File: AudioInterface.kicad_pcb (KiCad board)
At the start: 6 copper layers, 0 parts

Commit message: place component on pcb to generate bom
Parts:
- added D1: SML-P11UTT86R, LED_SMD:LED_0402_1005Metric, F.Cu at (146.7, 109.0)
- added D2: 1N4148, Diode_THT:D_DO-35_SOD27_P7.62mm_Horizontal, F.Cu at (154.9, 96.7)
- added D3: SML-P11MTT86RH, LED_SMD:LED_0402_1005Metric, F.Cu at (171.5, 90.3)
- added J3: PJ-393-8P, 0__:AUDIO-TH_PJ-393-8A, F.Cu at (143.8, 85.4)
- added J4: PJ-603, 0__:AUDIO-TH_PJ-603, F.Cu at (163.4, 69.6)
- added JP1: SolderJumper_2_Open, Jumper:SolderJumper-2_P1.3mm_Open_TrianglePad1.0x1.5mm, F.Cu at (151.2, 79.0)
- added JP2: SolderJumper_2_Open, Jumper:SolderJumper-2_P1.3mm_Open_TrianglePad1.0x1.5mm, F.Cu at (151.2, 82.5)
- added JP3: SolderJumper_2_Open, Jumper:SolderJumper-2_P1.3mm_Open_TrianglePad1.0x1.5mm, F.Cu at (151.2, 86.1)
- added JP4: SolderJumper_2_Open, Jumper:SolderJumper-2_P1.3mm_Open_TrianglePad1.0x1.5mm, F.Cu at (151.2, 89.6)
- added JP5: SolderJumper_2_Open, Jumper:SolderJumper-2_P1.3mm_Open_TrianglePad1.0x1.5mm, F.Cu at (151.2, 93.2)
- added JP6: SolderJumper_2_Open, Jumper:SolderJumper-2_P1.3mm_Open_TrianglePad1.0x1.5mm, F.Cu at (151.2, 96.7)
- added K1: IM03DGR, 0__:RELAY_IM03DGR, F.Cu at (159.1, 89.4)
- added Q1: AONS21321, 0__:DFN-8_L6.0-W5.0-P1.27-LS6.2-BL, F.Cu at (141.9, 104.2)
- added Q2: BC817, Package_TO_SOT_SMD:SOT-23, F.Cu at (167.3, 91.7)
- added S1: PG151101S11, 0__:SW_PG151101S11, F.Cu at (162.6, 80.9)
- added U2: ATTINY9-TS8R, 0__:SOT95P270X145-6N, F.Cu at (167.6, 87.0)
- added U3: L78L05ABUTR, 0__:L78L05ABUTR, F.Cu at (148.8, 104.0)
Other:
- board outline added: 71.5 x 73.5 mm

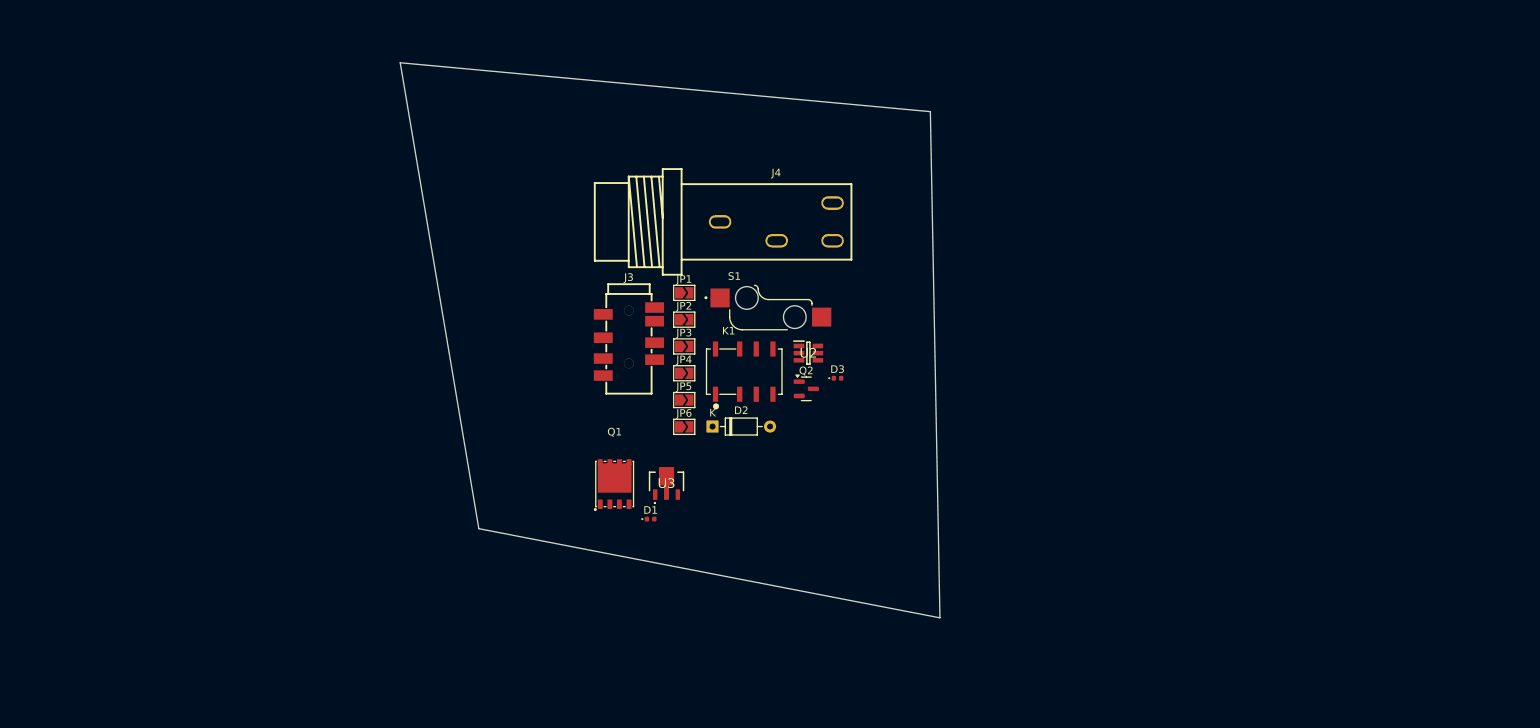
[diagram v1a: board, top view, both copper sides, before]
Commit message: source component and fix some lib
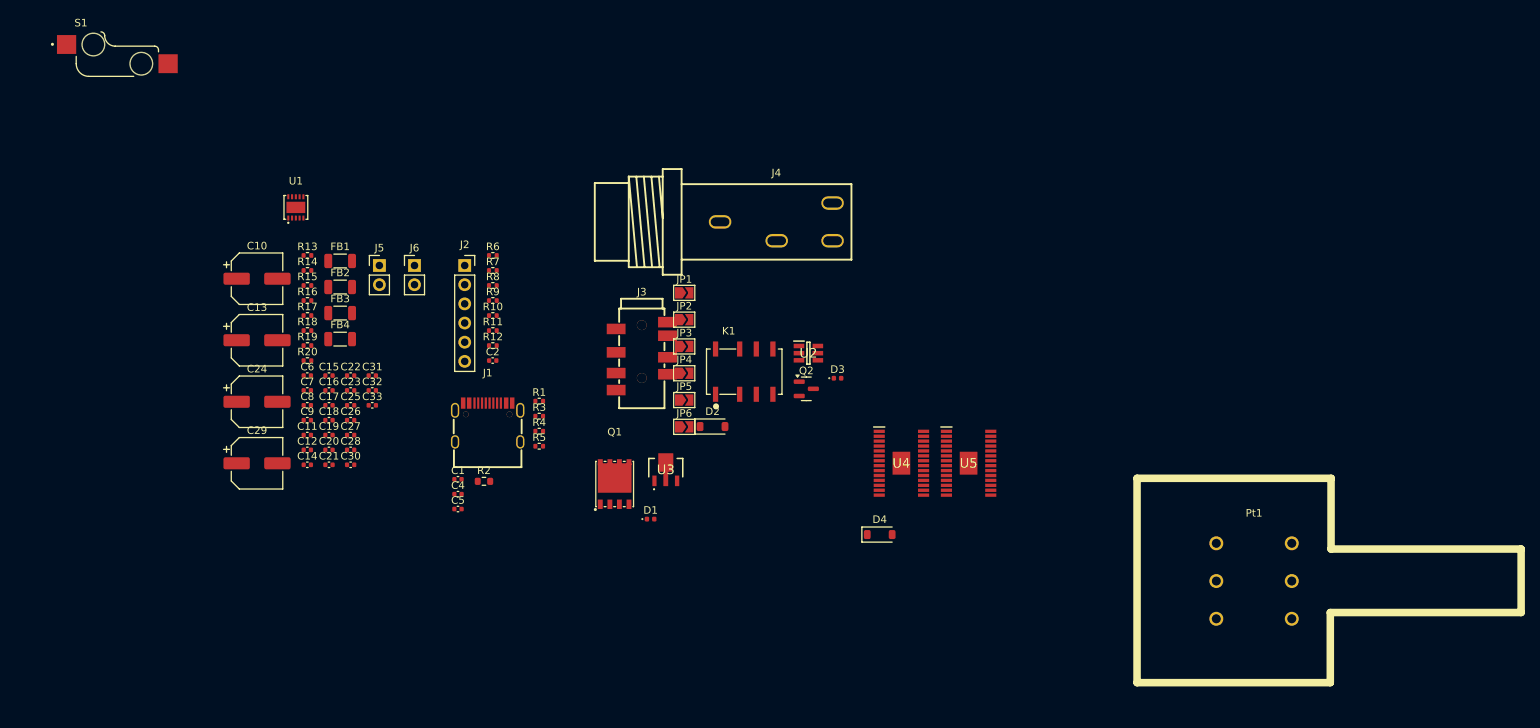
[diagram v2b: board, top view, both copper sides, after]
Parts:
- added C1: 1µ, Capacitor_SMD:C_0402_1005Metric, F.Cu at (121.2, 103.7)
- added C10: 100µ, Capacitor_SMD:CP_Elec_6.3x7.7, F.Cu at (94.6, 77.1)
- added C11: 100n, Capacitor_SMD:C_0402_1005Metric, F.Cu at (101.2, 97.8)
- added C12: 1n, Capacitor_SMD:C_0402_1005Metric, F.Cu at (101.2, 99.8)
- added C13: 100µ, Capacitor_SMD:CP_Elec_6.3x7.7, F.Cu at (94.6, 85.3)
- added C14: 100n, Capacitor_SMD:C_0402_1005Metric, F.Cu at (101.2, 101.8)
- added C15: 1n, Capacitor_SMD:C_0402_1005Metric, F.Cu at (104.1, 90.0)
- added C16: 100n, Capacitor_SMD:C_0402_1005Metric, F.Cu at (104.1, 91.9)
- added C17: 100n, Capacitor_SMD:C_0402_1005Metric, F.Cu at (104.1, 93.9)
- added C18: 1n, Capacitor_SMD:C_0402_1005Metric, F.Cu at (104.1, 95.9)
- added C19: 1n, Capacitor_SMD:C_0402_1005Metric, F.Cu at (104.1, 97.8)
- added C2: 100n, Capacitor_SMD:C_0402_1005Metric, F.Cu at (125.8, 88.0)
- added C20: 1µ, Capacitor_SMD:C_0402_1005Metric, F.Cu at (104.1, 99.8)
- added C21: 1µ, Capacitor_SMD:C_0402_1005Metric, F.Cu at (104.1, 101.8)
- added C22: 1µ, Capacitor_SMD:C_0402_1005Metric, F.Cu at (107.0, 90.0)
- added C23: 1µ, Capacitor_SMD:C_0402_1005Metric, F.Cu at (107.0, 91.9)
- added C24: 100µ, Capacitor_SMD:CP_Elec_6.3x7.7, F.Cu at (94.6, 93.4)
- added C25: 100n, Capacitor_SMD:C_0402_1005Metric, F.Cu at (107.0, 93.9)
- added C26: 100n, Capacitor_SMD:C_0402_1005Metric, F.Cu at (107.0, 95.9)
- added C27: 100n, Capacitor_SMD:C_0402_1005Metric, F.Cu at (107.0, 97.8)
- added C28: 1n, Capacitor_SMD:C_0402_1005Metric, F.Cu at (107.0, 99.8)
- added C29: 100µ, Capacitor_SMD:CP_Elec_6.3x7.7, F.Cu at (94.6, 101.6)
- added C30: 100n, Capacitor_SMD:C_0402_1005Metric, F.Cu at (107.0, 101.8)
- added C31: 1n, Capacitor_SMD:C_0402_1005Metric, F.Cu at (109.8, 90.0)
- added C32: 1n, Capacitor_SMD:C_0402_1005Metric, F.Cu at (109.8, 91.9)
- added C33: 1n, Capacitor_SMD:C_0402_1005Metric, F.Cu at (109.8, 93.9)
- added C4: 330n, Capacitor_SMD:C_0402_1005Metric, F.Cu at (121.2, 105.7)
- added C5: 100n, Capacitor_SMD:C_0402_1005Metric, F.Cu at (121.2, 107.6)
- added C6: 1µ, Capacitor_SMD:C_0402_1005Metric, F.Cu at (101.2, 90.0)
- added C7: 1µ, Capacitor_SMD:C_0402_1005Metric, F.Cu at (101.2, 91.9)
- added C8: 1µ, Capacitor_SMD:C_0402_1005Metric, F.Cu at (101.2, 93.9)
- added C9: 1µ, Capacitor_SMD:C_0402_1005Metric, F.Cu at (101.2, 95.9)
- added D4: 1N4148, Diode_SMD:D_SOD-123, F.Cu at (177.1, 111.0)
- added FB1: FBMJ3216HS800-TV, Inductor_SMD:L_1206_3216Metric, F.Cu at (105.6, 74.8)
- added FB2: FBMJ3216HS800-TV, Inductor_SMD:L_1206_3216Metric, F.Cu at (105.6, 78.2)
- added FB3: FBMJ3216HS800-TV, Inductor_SMD:L_1206_3216Metric, F.Cu at (105.6, 81.7)
- added FB4: FBMJ3216HS800-TV, Inductor_SMD:L_1206_3216Metric, F.Cu at (105.6, 85.1)
- added J1: TYPE-C 16PIN L8.35, 0__:TYPE-C-SMD_20009-UCAF001-X, F.Cu at (125.1, 96.2)
- added J2: AVR-ISP-6, Connector_PinSocket_2.54mm:PinSocket_1x06_P2.54mm_Vertical, F.Cu at (122.1, 75.4)
- added J5: Speaker ouput L, Connector_PinHeader_2.54mm:PinHeader_1x02_P2.54mm_Vertical, F.Cu at (110.8, 75.4)
- added J6: Speaker ouput R, Connector_PinHeader_2.54mm:PinHeader_1x02_P2.54mm_Vertical, F.Cu at (115.4, 75.4)
- added Pt1: RK27112A0A16, 0__:RES-ADJ-TH_RK27112A0A16, F.Cu at (226.6, 117.2)
- added R1: 10, Resistor_SMD:R_0402_1005Metric, F.Cu at (132.0, 93.3)
- added R10: 2.2k, Resistor_SMD:R_0402_1005Metric, F.Cu at (125.8, 82.0)
- added R11: 2.2k, Resistor_SMD:R_0402_1005Metric, F.Cu at (125.8, 84.0)
- added R12: 2.2k, Resistor_SMD:R_0402_1005Metric, F.Cu at (125.8, 86.0)
- added R13: 100k, Resistor_SMD:R_0402_1005Metric, F.Cu at (101.3, 74.0)
- added R14: 10, Resistor_SMD:R_0402_1005Metric, F.Cu at (101.3, 76.0)
- added R15: 100k, Resistor_SMD:R_0402_1005Metric, F.Cu at (101.3, 78.0)
- added R16: 1k, Resistor_SMD:R_0402_1005Metric, F.Cu at (101.3, 80.0)
- added R17: 1k, Resistor_SMD:R_0402_1005Metric, F.Cu at (101.3, 82.0)
- added R18: 10, Resistor_SMD:R_0402_1005Metric, F.Cu at (101.3, 84.0)
- added R19: 100k, Resistor_SMD:R_0402_1005Metric, F.Cu at (101.3, 86.0)
- added R2: 5.1k, Resistor_SMD:R_0603_1608Metric, F.Cu at (124.6, 104.0)
- added R20: 100k, Resistor_SMD:R_0402_1005Metric, F.Cu at (101.3, 88.0)
- added R3: 49.9k, Resistor_SMD:R_0402_1005Metric, F.Cu at (132.0, 95.3)
- added R4: 4.53k, Resistor_SMD:R_0402_1005Metric, F.Cu at (132.0, 97.3)
- added R5: 18k, Resistor_SMD:R_0402_1005Metric, F.Cu at (132.0, 99.3)
- added R6: 470k, Resistor_SMD:R_0402_1005Metric, F.Cu at (125.8, 74.0)
- added R7: 330, Resistor_SMD:R_0402_1005Metric, F.Cu at (125.8, 76.0)
- added R8: 150, Resistor_SMD:R_0402_1005Metric, F.Cu at (125.8, 78.0)
- added R9: 2.2k, Resistor_SMD:R_0402_1005Metric, F.Cu at (125.8, 80.0)
- added U1: HUSB238_002DD, 0__:DFN-10_L3.0-W3.0-P0.50-BL-EP2.5, F.Cu at (99.7, 67.7)
- added U4: TPA3111D1QPWPRQ1, 0__:SOP65P640X120-29N, F.Cu at (179.9, 101.6)
- added U5: TPA3111D1QPWPRQ1, 0__:SOP65P640X120-29N, F.Cu at (188.8, 101.6)
- D2: footprint Diode_THT:D_DO-35_SOD27_P7.62mm_Horizontal -> Diode_SMD:D_SOD-123
- moved S1 92.9 mm to (76.1, 47.4)
- moved J3 2.57 mm to (145.5, 87.4)
- moved U3 1.82 mm to (148.7, 102.2)
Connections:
- K1 pad 4: /Project Architecture/Output Selector/To_Amplifier_L -> /Project Architecture/Amplifier/From_Selector_L
- K1 pad 5: /Project Architecture/Output Selector/To_Amplifier_R -> /Project Architecture/Amplifier/From_Selector_R
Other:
- board outline removed

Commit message: add connector to separate the selector switch and led indicator
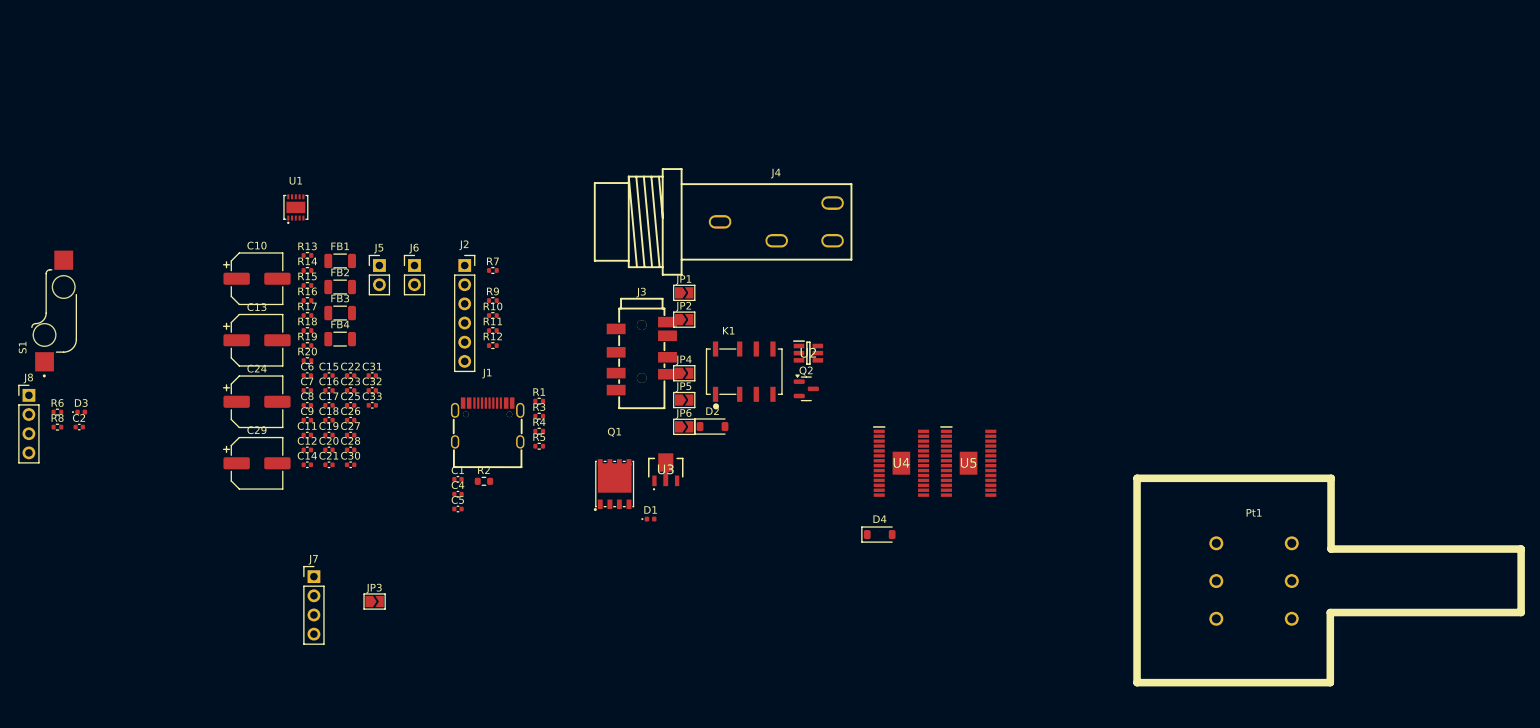
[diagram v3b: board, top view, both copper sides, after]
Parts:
- added J7: ToFront, Connector_PinHeader_2.54mm:PinHeader_1x04_P2.54mm_Vertical, F.Cu at (102.1, 116.6)
- added J8: FromMotherboard, Connector_PinHeader_2.54mm:PinHeader_1x04_P2.54mm_Vertical, F.Cu at (64.4, 92.6)
- moved D3 100.3 mm to (71.3, 94.8)
- moved R6 61.3 mm to (68.1, 94.8)
- moved R8 60.7 mm to (68.1, 96.8)
- moved C2 55.5 mm to (71.0, 96.8)
- moved JP3 53.1 mm to (110.1, 119.9)
- moved S1 35.0 mm to (67.7, 81.4), turned to 90 degrees
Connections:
- C2 pad 1: GND -> GND1
- C2 pad 2: Net-(JP1-A) -> Net-(J8-Pin_3)
- D3 pad 1: GND -> GND1
- JP1 pad 1: Net-(JP1-A) -> Net-(J7-Pin_3)
- JP3 pad 1: /Project Architecture/Output Selector/SCK -> /Project Architecture/Output Selector/SS
- JP3 pad 2: Net-(JP3-B) -> Net-(J7-Pin_2)
- R6 pad 1: +5V -> +5C
- R8 pad 1: Net-(JP3-B) -> Net-(J8-Pin_2)
- S1 pad 2: Net-(JP1-A) -> Net-(J8-Pin_3)

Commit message: finish pcb and generate production file
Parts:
- added G***: LOGO, LOGO, F.Cu at (119.4, 84.6)
- added H1: MountingHole_Pad, MountingHole:MountingHole_3.2mm_M3_Pad_Via, F.Cu at (108.5, 79.8)
- added H2: MountingHole_Pad, MountingHole:MountingHole_3.2mm_M3_Pad_Via, F.Cu at (108.5, 129.5)
- added H3: MountingHole_Pad, MountingHole:MountingHole_3.2mm_M3_Pad_Via, F.Cu at (170.7, 129.5)
- added H4: MountingHole_Pad, MountingHole:MountingHole_3.2mm_M3_Pad_Via, F.Cu at (170.7, 79.8)
- added H5: MountingHole_Pad, MountingHole:MountingHole_3.2mm_M3_Pad_Via, F.Cu at (139.7, 64.8)
- added H6: MountingHole_Pad, MountingHole:MountingHole_3.2mm_M3_Pad_Via, F.Cu at (168.7, 64.8)
- J2: footprint Connector_PinSocket_2.54mm:PinSocket_1x06_P2.54mm_Vertical -> Connector_PinSocket_2.54mm:PinSocket_2x03_P2.54mm_Vertical
- S1: footprint 0__:SW_PG151101S11 -> 0__:Kailh_socket_MX
- moved J8 101.3 mm to (162.8, 68.8), turned to 180 degrees
- moved R8 98.2 mm to (159.5, 60.7), turned to 90 degrees
- moved R6 94.8 mm to (159.5, 69.6), turned to -90 degrees
- moved C2 93.2 mm to (159.5, 67.6), turned to -90 degrees
- moved D3 86.6 mm to (150.6, 60.2)
- moved S1 84.5 mm to (150.6, 65.0), turned to 180 degrees
- moved C10 63.5 mm to (130.8, 129.3)
- moved Pt1 61.4 mm to (165.4, 111.8)
- moved R15 58.5 mm to (137.7, 123.8), turned to 180 degrees
- moved R14 58.2 mm to (137.7, 121.4)
- moved R16 57.8 mm to (137.7, 124.8)
- moved U5 56.7 mm to (132.5, 95.2), turned to 180 degrees
- moved R13 55.8 mm to (137.6, 116.3)
- moved U4 51.1 mm to (132.5, 120.4), turned to 180 degrees
- moved FB1 50.9 mm to (124.2, 122.2), turned to 180 degrees
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- renumbered C25 to C24, C26 to C25, C24 to C26
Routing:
- net VCC: track 0.00 -> 143.4 mm, vias 0 -> 7
- net +5V: track 0.00 -> 56.4 mm, vias 0 -> 4
- net Net-(J3-Pad3): track 0.00 -> 44.7 mm
- net Net-(C20-Pad1): track 0.00 -> 40.4 mm, vias 0 -> 1
- net Net-(J4-Pad3): track 0.00 -> 40.4 mm
- net /Project Architecture/Amplifier/~{AmpSD}: track 0.00 -> 38.7 mm, vias 0 -> 3
- net Net-(J3-Pad2): track 0.00 -> 33.9 mm
- net GND: track 0.00 -> 32.6 mm, vias 0 -> 1
- net /Project Architecture/Amplifier/From_Selector_R: track 0.00 -> 29.2 mm
- net /Project Architecture/Amplifier/From_Selector_L: track 0.00 -> 25.1 mm
- net Net-(C8-Pad1): track 0.00 -> 24.8 mm
- net Net-(J4-Pad5): track 0.00 -> 22.5 mm
- net GND1: track 0.00 -> 19.2 mm, vias 0 -> 1
- net Net-(R6-Pad2): track 0.00 -> 18.0 mm, vias 0 -> 1
- net /Project Architecture/Output Selector/MISO: track 0.00 -> 16.2 mm, vias 0 -> 2
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- added copper zone on B.Cu, net GND
- added copper zone on F.Cu, net GND
- added copper zone on B.Cu, net GND1
- added copper zone on F.Cu, net GND1
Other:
- board outline added: 72.4 x 78.7 mm
- copper layers 6 -> 2
- board text added: "Audio Interface Amplifier 2x10 W"
- board text added: "Input"
- board text added: "JLCJLCJLCJLC"
- board text added: "OUT L"
- board text added: "OUT R"
- board text added: "Output 1"
